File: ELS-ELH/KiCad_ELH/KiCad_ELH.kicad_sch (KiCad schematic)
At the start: 38 parts, among them J1 Pressure Transducer Screw Ter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, J2 Conn_01x09_Pin, J8 RW1 Screw Terminal, Q1 IRLZ44N, Q2 IRLZ44N, Q4 IRLZ44N, Q6 IRLZ44N

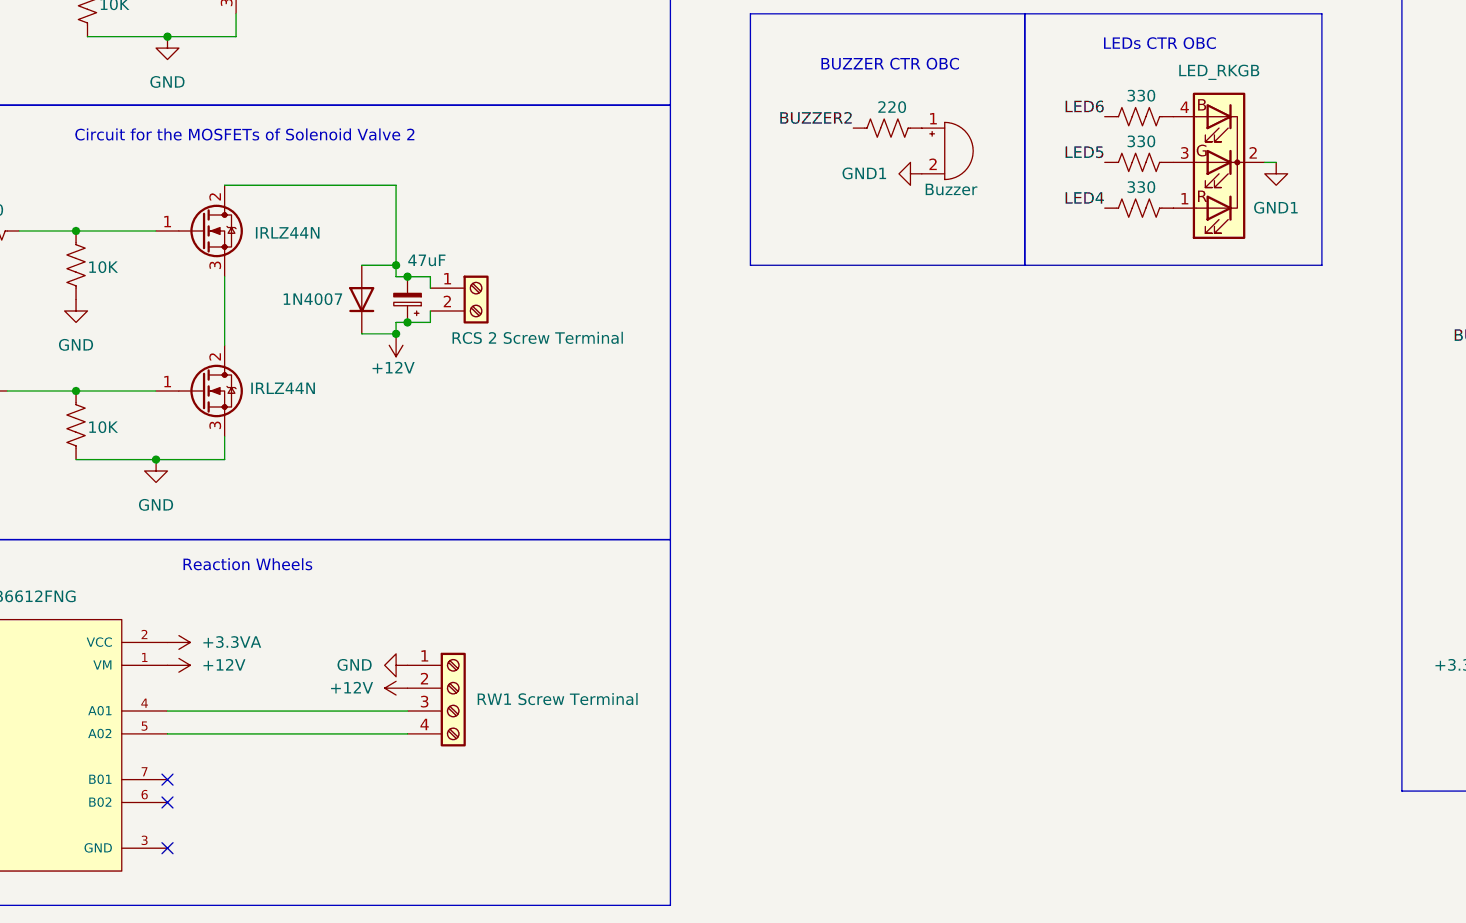
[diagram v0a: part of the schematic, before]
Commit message: Editing some footprints and connections
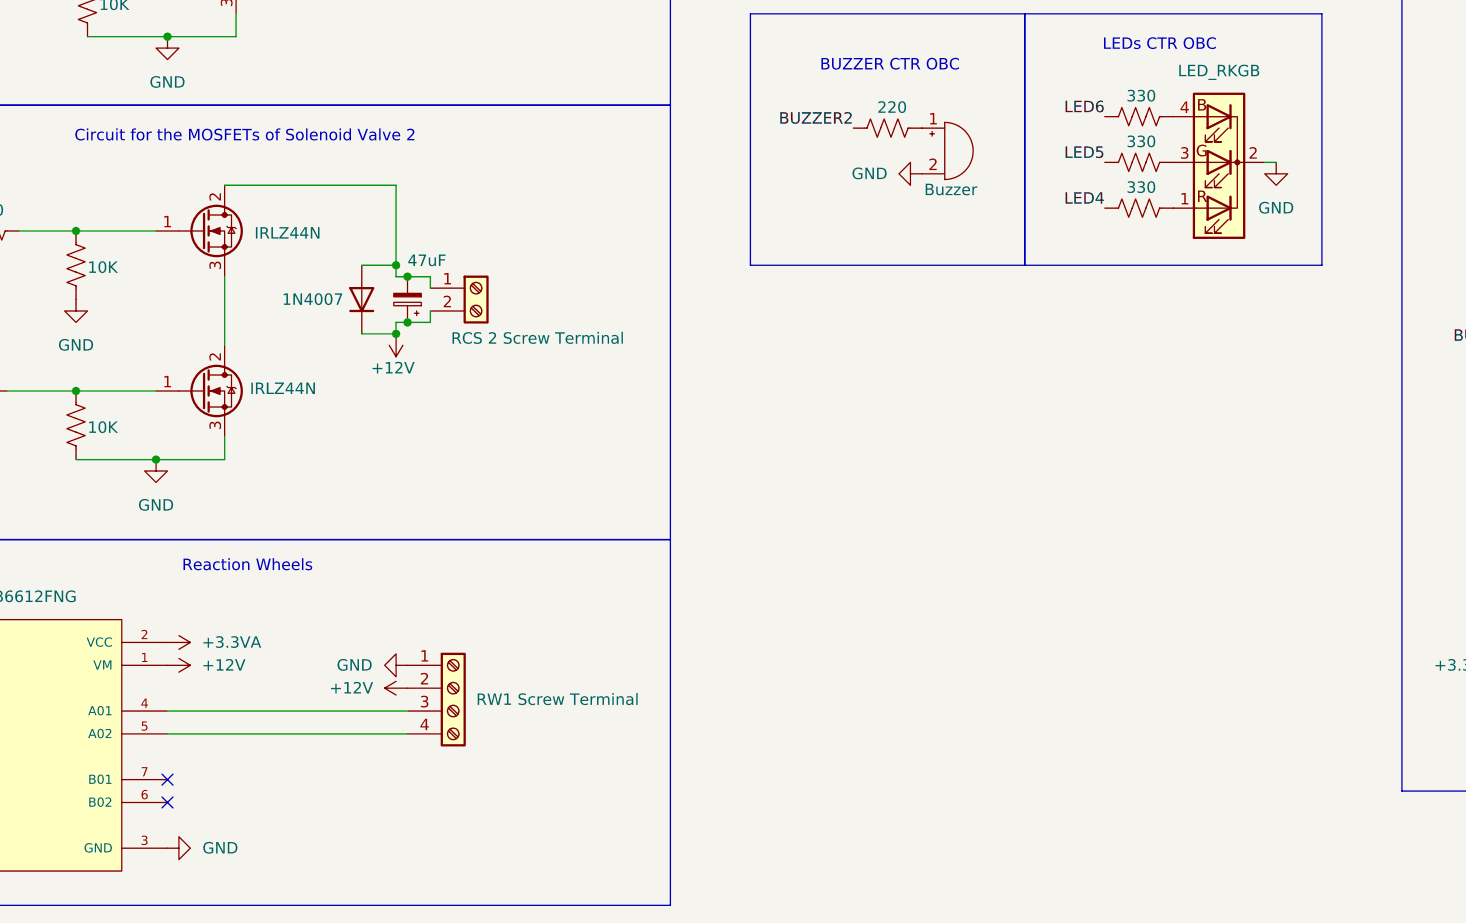
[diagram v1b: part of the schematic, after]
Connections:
- net GND1 is gone; now on net GND: BZ2.2 (-), D3.2 (K)
- no-connect marks 44 -> 43
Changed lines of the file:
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@@
 	)
 	(no_connect
-		(at 55.88 168.91)
-	)
-	(no_connect
 		(at 207.01 107.95)
 	)
@@
 	)
 	(symbol
-		(lib_id "power:GND1")
-		(at 179.07 92.71 0)
-		(unit 1)
-		(exclude_from_sim no)
-		(in_bom yes)
-		(on_board yes)
-		(dnp no)
-		(fields_autoplaced yes)
-		(property "Reference" "#PWR020"
-			(at 179.07 99.06 0)
-			(effects
-				(font
-					(size 1.27 1.27)
-				)
-				(hide yes)
-			)
-		)
-		(property "Value" "GND1"
-			(at 179.07 97.79 0)
-			(effects
-				(font
-					(size 1.27 1.27)
-				)
-			)
-		)
-		(property "Footprint" ""
-			(at 179.07 92.71 0)
-			(effects
-				(font
-					(size 1.27 1.27)
-				)
-				(hide yes)
-			)
-		)
-		(property "Datasheet" ""
-			(at 179.07 92.71 0)
-			(effects
-				(font
-					(size 1.27 1.27)
-				)
-				(hide yes)
-			)
-		)
-		(property "Description" "Power symbol creates a global label with name \"GND1\" , ground"
-			(at 179.07 92.71 0)
-			(effects
-				(font
-					(size 1.27 1.27)
-				)
-				(hide yes)
-			)
-		)
-		(pin "1"
-		)
-		(instances
-			(project "KiCad_ELH"
-				(path "/d2c6e293-9221-4377-94b4-35f6301c1d6b"
-					(reference "#PWR020")
-					(unit 1)
-				)
-			)
-		)
-	)
-	(symbol
 		(lib_id "power:+12V")
 		(at 82.55 151.13 90)
@@
 	(symbol
 		(lib_id "power:GND")
+		(at 179.07 92.71 0)
+		(unit 1)
+		(exclude_from_sim no)
+		(in_bom yes)
+		(on_board yes)
+		(dnp no)
+		(fields_autoplaced yes)
+		(property "Reference" "#PWR020"
+			(at 179.07 99.06 0)
+			(effects
+				(font
+					(size 1.27 1.27)
+				)
+				(hide yes)
+			)
+		)
+		(property "Value" "GND"
+			(at 179.07 97.79 0)
+			(effects
+				(font
+					(size 1.27 1.27)
+				)
+			)
+		)
+		(property "Footprint" ""
+			(at 179.07 92.71 0)
+			(effects
+				(font
+					(size 1.27 1.27)
+				)
+				(hide yes)
+			)
+		)
+		(property "Datasheet" ""
+			(at 179.07 92.71 0)
+			(effects
+				(font
+					(size 1.27 1.27)
+				)
+				(hide yes)
+			)
+		)
+		(property "Description" "Power symbol creates a global label with name \"GND\" , ground"
+			(at 179.07 92.71 0)
+			(effects
+				(font
+					(size 1.27 1.27)
+				)
+				(hide yes)
+			)
+		)
+		(pin "1"
+		)
+		(instances
+			(project "KiCad_ELH"
+				(path "/d2c6e293-9221-4377-94b4-35f6301c1d6b"
+					(reference "#PWR020")
+					(unit 1)
+				)
+			)
+		)
+	)
+	(symbol
+		(lib_id "power:GND")
 		(at 148.59 67.31 90)
 		(unit 1)
@@
 	)
 	(symbol
-		(lib_id "power:GND1")
-		(at 139.7 93.98 270)
-		(unit 1)
-		(exclude_from_sim no)
-		(in_bom yes)
-		(on_board yes)
-		(dnp no)
-		(fields_autoplaced yes)
-		(property "Reference" "#PWR024"
-			(at 133.35 93.98 0)
-			(effects
-				(font
-					(size 1.27 1.27)
-				)
-				(hide yes)
-			)
-		)
-		(property "Value" "GND1"
-			(at 135.89 93.9799 90)
-			(effects
-				(font
-					(size 1.27 1.27)
-				)
-				(justify right)
-			)
-		)
-		(property "Footprint" ""
-			(at 139.7 93.98 0)
-			(effects
-				(font
-					(size 1.27 1.27)
-				)
-				(hide yes)
-			)
-		)
-		(property "Datasheet" ""
-			(at 139.7 93.98 0)
-			(effects
-				(font
-					(size 1.27 1.27)
-				)
-				(hide yes)
-			)
-		)
-		(property "Description" "Power symbol creates a global label with name \"GND1\" , ground"
-			(at 139.7 93.98 0)
-			(effects
-				(font
-					(size 1.27 1.27)
-				)
-				(hide yes)
-			)
-		)
-		(pin "1"
-		)
-		(instances
-			(project "KiCad_ELH"
-				(path "/d2c6e293-9221-4377-94b4-35f6301c1d6b"
-					(reference "#PWR024")
-					(unit 1)
-				)
-			)
-		)
-	)
-	(symbol
 		(lib_id "Diode:1N4007")
 		(at 77.47 107.95 90)
@@
 	)
 	(symbol
+		(lib_id "power:GND1")
+		(at 55.88 168.91 90)
+		(unit 1)
+		(exclude_from_sim no)
+		(in_bom yes)
+		(on_board yes)
+		(dnp no)
+		(property "Reference" "#PWR047"
+			(at 62.23 168.91 0)
+			(effects
+				(font
+					(size 1.27 1.27)
+				)
+				(hide yes)
+			)
+		)
+		(property "Value" "GND"
+			(at 63.754 168.91 90)
+			(effects
+				(font
+					(size 1.27 1.27)
+				)
+				(justify left)
+			)
+		)
+		(property "Footprint" ""
+			(at 55.88 168.91 0)
+			(effects
+				(font
+					(size 1.27 1.27)
+				)
+				(hide yes)
+			)
+		)
+		(property "Datasheet" ""
+			(at 55.88 168.91 0)
+			(effects
+				(font
+					(size 1.27 1.27)
+				)
+				(hide yes)
+			)
+		)
+		(property "Description" "Power symbol creates a global label with name \"GND1\" , ground"
+			(at 55.88 168.91 0)
+			(effects
+				(font
+					(size 1.27 1.27)
+				)
+				(hide yes)
+			)
+		)
+		(pin "1"
+		)
+		(instances
+			(project "KiCad_ELH"
+				(path "/d2c6e293-9221-4377-94b4-35f6301c1d6b"
+					(reference "#PWR047")
+					(unit 1)
+				)
+			)
+		)
+	)
+	(symbol
 		(lib_id "power:+12V")
 		(at 81.28 64.77 180)
@@
 					(unit 1)
 				)
+			)
+		)
+	)
+	(symbol
+		(lib_id "power:GND")
+		(at 139.7 93.98 270)
+		(unit 1)
+		(exclude_from_sim no)
+		(in_bom yes)
+		(on_board yes)
+		(dnp no)
+		(fields_autoplaced yes)
+		(property "Reference" "#PWR024"
+			(at 133.35 93.98 0)
+			(effects
+				(font
+					(size 1.27 1.27)
+				)
+				(hide yes)
+			)
+		)
+		(property "Value" "GND"
+			(at 135.89 93.9799 90)
+			(effects
+				(font
+					(size 1.27 1.27)
+				)
+				(justify right)
+			)
+		)
+		(property "Footprint" ""
+			(at 139.7 93.98 0)
+			(effects
+				(font
+					(size 1.27 1.27)
+				)
+				(hide yes)
+			)
+		)
+		(property "Datasheet" ""
+			(at 139.7 93.98 0)
+			(effects
+				(font
+					(size 1.27 1.27)
+				)
+				(hide yes)
+			)
+		)
+		(property "Description" "Power symbol creates a global label with name \"GND\" , ground"
+			(at 139.7 93.98 0)
+			(effects
+				(font
+					(size 1.27 1.27)
+				)
+				(hide yes)
+			)
+		)
+		(pin "1"
+		)
+		(instances
+			(project "KiCad_ELH"
+				(path "/d2c6e293-9221-4377-94b4-35f6301c1d6b"
+					(reference "#PWR024")
+					(unit 1)
+				)
